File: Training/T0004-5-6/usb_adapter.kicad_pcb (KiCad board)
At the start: 2 copper layers, 50.8 x 25.4 mm, 23 parts, among them J1 modular8_rev3_comms_out, P1 USB_OTG, U1 FT231X, U2 TE_1825058-1

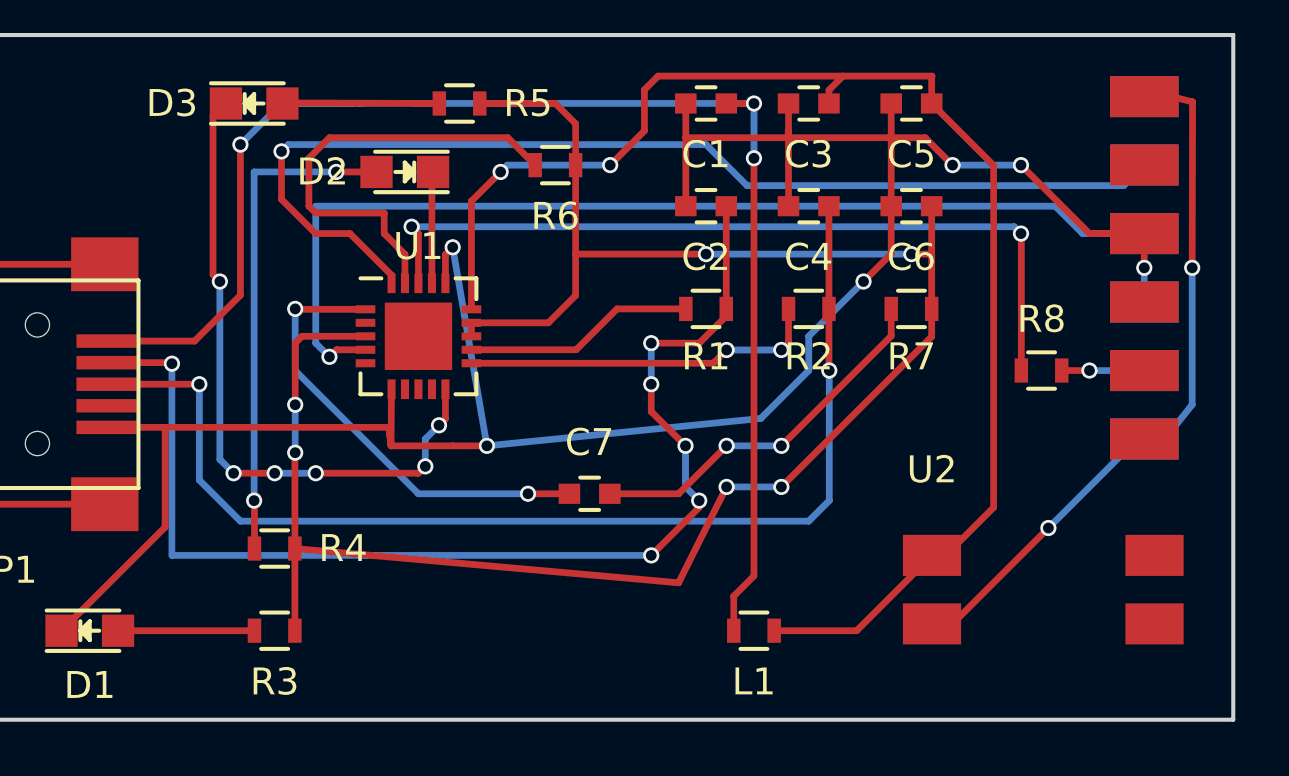
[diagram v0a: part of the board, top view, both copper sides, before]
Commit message: footprint updates and comments
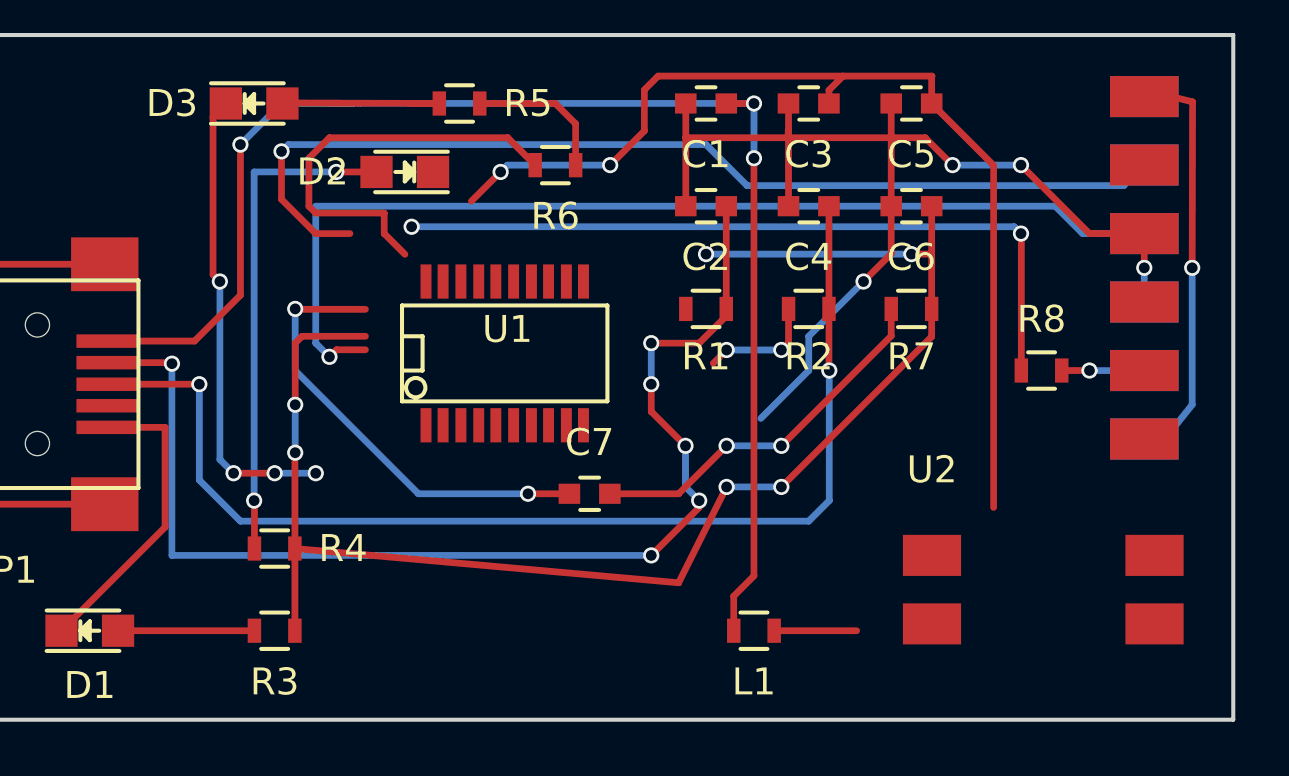
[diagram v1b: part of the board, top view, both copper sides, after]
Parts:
- U1: footprint Housings_DFN_QFN:QFN-20-1EP_4x4mm_Pitch0.5mm -> SMD_Packages:SSOP-20
- moved U1 3.26 mm to (161.7, 87.8)
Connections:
- U2 pad 1: +5V -> /POWER_OUT
- U2 pad 2: /POWER_OUT -> Net-(J1-Pad7)
- U2 pad 3: (no net) -> /PROGRAM
- U2 pad 4: (no net) -> +5V
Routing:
- net GND: track 88.7 -> 54.2 mm, vias 6 -> 4
- net +3V3: track 74.7 -> 60.2 mm
- net +5V: track 52.1 -> 41.1 mm
- net /POWER_OUT: track 26.2 -> 16.2 mm, vias 2 -> 1
- net Net-(R2-Pad1): track 13.3 -> 4.36 mm
- net Net-(R1-Pad1): track 8.58 -> 0.00 mm
- net /~TXLED: track 24.6 -> 17.3 mm, vias 6 -> 4
- net /~RXLED: track 4.15 -> 0.06 mm
- net /TX: track 40.4 -> 37.9 mm
- net /TXDEN: track 30.0 -> 27.8 mm
- net /~SLEEP: track 16.7 -> 15.7 mm
- net Net-(J1-Pad7): track 0.00 -> 0.76 mm

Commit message: finished routing after fix
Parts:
- moved C1 26.0 mm to (153.9, 99.6), turned to 270 degrees
- moved R4 24.9 mm to (178.1, 95.8), turned to 90 degrees
- moved C5 24.0 mm to (165.4, 99.6), turned to 270 degrees
- moved C4 23.6 mm to (156.2, 98.9), turned to 270 degrees
- moved R5 23.4 mm to (175.8, 95.8), turned to 90 degrees
- moved C6 23.1 mm to (160.8, 98.9), turned to 270 degrees
- moved D1 23.1 mm to (169.3, 96.0), turned to 90 degrees
- moved C3 22.7 mm to (163.1, 98.9), turned to 270 degrees
- moved R3 20.4 mm to (173.5, 95.8), turned to 90 degrees
- moved C2 19.8 mm to (158.5, 98.9), turned to 270 degrees
- moved D2 19.4 mm to (177.4, 80.4), turned to 0 degrees
- moved R2 19.4 mm to (156.0, 95.5), turned to 270 degrees
- moved D3 19.4 mm to (171.7, 80.4)
- moved L1 17.7 mm to (158.4, 85.6), turned to 270 degrees
- moved C7 17.1 mm to (181.9, 91.7)
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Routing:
- net Net-(C1-Pad1): track 51.8 -> 18.6 mm, vias 3 -> 2
- net Net-(C4-Pad1): track 42.2 -> 11.7 mm, vias 2 -> 0
- net Net-(C2-Pad1): track 43.9 -> 15.5 mm, vias 6 -> 0
- net /~RXLED: track 0.06 -> 20.2 mm, vias 0 -> 2
- net Net-(R1-Pad1): track 0.00 -> 18.6 mm, vias 0 -> 2
- net Net-(R2-Pad1): track 4.36 -> 22.0 mm
- net /RX: track 38.4 -> 22.2 mm
- net GND: track 54.2 -> 68.8 mm
- net /~TXLED: track 17.3 -> 2.82 mm, vias 4 -> 0
- net /POWER_OUT: track 16.2 -> 29.8 mm, vias 1 -> 2
- net Net-(J1-Pad7): track 0.76 -> 14.2 mm
- net /TXDEN: track 27.8 -> 15.3 mm
- net Net-(D3-Pad2): track 5.84 -> 17.0 mm, vias 0 -> 2
- net +3V3: track 60.2 -> 49.4 mm
- net /PROGRAM: track 13.9 -> 7.26 mm, vias 2 -> 0
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
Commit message: generated gerbers
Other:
- board text added: "USB to serial Jeremy OpenRobotics.ca"
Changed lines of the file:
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@@
     (area 142.164999 74.48957 195.793 104.48)
     (thickness 1.6)
-    (drawings 4)
+    (drawings 5)
     (tracks 202)
     (zones 0)
@@
     (visible_elements 7FFEFF7F)
     (pcbplotparams
-      (layerselection 0x00030_80000001)
-      (usegerberextensions false)
+      (layerselection 0x010f0_80000001)
+      (usegerberextensions true)
       (excludeedgelayer true)
       (linewidth 0.100000)
@@
       (outputformat 1)
       (mirror false)
-      (drillshape 1)
+      (drillshape 0)
       (scaleselection 1)
-      (outputdirectory ""))
+      (outputdirectory ../gerbers/Jeremy/))
   )
   (net 0 "")
@@
     (pad 4 smd rect (at 8.255 0 180) (size 2.159 1.524) (layers F.Cu F.Paste F.Mask)
       (net 4 +5V))
+  )
+  (gr_text "USB to serial\nJeremy\nOpenRobotics.ca" (at 143.256 80.264 180) (layer B.SilkS)
+    (effects (font (size 1 1) (thickness 0.1)) (justify left mirror))
   )
   (gr_line (start 193.04 76.962) (end 142.24 76.962) (angle 90) (layer Edge.Cuts) (width 0.15))
@@
   (segment (start 169.291 94.96298) (end 173.43698 94.96298) (width 0.25) (layer F.Cu) (net 9))
   (segment (start 173.43698 94.96298) (end 173.482 95.008) (width 0.25) (layer F.Cu) (net 9))
-  (segment (start 178.46802 80.391) (end 178.46802 84.67598) (width 0.25) (layer F.Cu) (net 10) (status 400000))
-  (segment (start 178.054 92.583) (end 178.054 95.008) (width 0.25) (layer F.Cu) (net 10) (status 800000))
+  (segment (start 178.46802 80.391) (end 178.46802 84.67598) (width 0.25) (layer F.Cu) (net 10))
+  (segment (start 178.054 92.583) (end 178.054 95.008) (width 0.25) (layer F.Cu) (net 10))
   (via (at 178.054 92.583) (size 0.6) (drill 0.4) (layers F.Cu B.Cu) (net 10))
   (segment (start 178.054 85.09) (end 178.054 92.583) (width 0.25) (layer B.Cu) (net 10))
@@
   (via (at 164.338 86.36) (size 0.6) (drill 0.4) (layers F.Cu B.Cu) (net 11))
   (segment (start 164.7952 86.8172) (end 164.338 86.36) (width 0.25) (layer F.Cu) (net 11))
-  (segment (start 172.75302 80.391) (end 174.625 80.391) (width 0.25) (layer F.Cu) (net 12) (status 400000))
-  (segment (start 175.768 92.583) (end 175.768 95.008) (width 0.25) (layer F.Cu) (net 12) (status 800000))
+  (segment (start 172.75302 80.391) (end 174.625 80.391) (width 0.25) (layer F.Cu) (net 12))
+  (segment (start 175.768 92.583) (end 175.768 95.008) (width 0.25) (layer F.Cu) (net 12))
   (via (at 175.768 92.583) (size 0.6) (drill 0.4) (layers F.Cu B.Cu) (net 12))
   (segment (start 175.768 85.471) (end 175.768 92.583) (width 0.25) (layer B.Cu) (net 12))
@@
   (segment (start 162.052 88.138) (end 165.989 88.138) (width 0.25) (layer F.Cu) (net 27))
   (segment (start 160.782 89.408) (end 162.052 88.138) (width 0.25) (layer F.Cu) (net 27))
-  (segment (start 165.989 87.4776) (end 168.2496 87.4776) (width 0.25) (layer F.Cu) (net 28) (status 400000))
-  (segment (start 174.244 87.122) (end 181.114 87.122) (width 0.25) (layer F.Cu) (net 28) (status 800000))
+  (segment (start 165.989 87.4776) (end 168.2496 87.4776) (width 0.25) (layer F.Cu) (net 28))
+  (segment (start 174.244 87.122) (end 181.114 87.122) (width 0.25) (layer F.Cu) (net 28))
   (segment (start 173.99 87.376) (end 174.244 87.122) (width 0.25) (layer F.Cu) (net 28))
   (via (at 173.99 87.376) (size 0.6) (drill 0.4) (layers F.Cu B.Cu) (net 28))

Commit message: generated gerbers
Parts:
- U1: value FT231X -> FT231XQ; footprint SMD_Packages:SSOP-20 -> Housings_DFN_QFN:QFN-20-1EP_4x4mm_Pitch0.5mm
- moved U2 49.9 mm to (141.0, 92.7), turned to 0 degrees
- moved C7 49.1 mm to (133.1, 85.9), turned to 90 degrees
- moved D2 49.1 mm to (133.1, 101.6)
- moved R4 48.7 mm to (130.3, 105.4)
- moved R3 46.7 mm to (127.8, 105.4)
- moved R7 44.9 mm to (140.4, 106.7)
- moved R5 44.0 mm to (132.8, 105.4)
- moved D3 40.7 mm to (136.9, 101.6)
- moved D1 40.4 mm to (129.3, 101.6), turned to 180 degrees
- moved C5 40.1 mm to (128.3, 84.3), turned to 90 degrees
- moved C3 40.0 mm to (125.7, 84.6), turned to 90 degrees
- moved U1 39.8 mm to (130.2, 96.1), turned to 270 degrees
- moved C2 38.1 mm to (123.2, 84.6), turned to 90 degrees
- moved R1 37.4 mm to (122.4, 105.4)
- moved R8 37.0 mm to (146.8, 99.1)
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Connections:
- U1 pad 1: Net-(C7-Pad1) -> /RX
- U1 pad 10: /~TXLED -> +3V3
- U1 pad 11: Net-(R2-Pad1) -> +3V3
- U1 pad 12: Net-(R1-Pad1) -> +5V
- U1 pad 13: +3V3 -> GND
- U1 pad 14: +3V3 -> /~RXLED
- U1 pad 15: +5V -> /TXDEN
- U1 pad 16: GND -> /~SLEEP
- U1 pad 17: /~RXLED -> /TX
- U1 pad 18: /TXDEN -> Net-(C7-Pad1)
- U1 pad 19: /~SLEEP -> Net-(U1-Pad19)
- U1 pad 20: /TX -> +3V3
- U1 pad 3: +3V3 -> GND
- U1 pad 4: /RX -> Net-(U1-Pad4)
- U1 pad 6: GND -> Net-(U1-Pad6)
- U1 pad 7: Net-(U1-Pad7) -> /~TXLED
- U1 pad 8: Net-(U1-Pad8) -> Net-(R2-Pad1)
- U1 pad 9: Net-(U1-Pad9) -> Net-(R1-Pad1)
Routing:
- net GND: track 68.8 -> 108.7 mm, vias 4 -> 6
- net /PROGRAM: track 7.26 -> 39.6 mm, vias 0 -> 3
- net /~TXLED: track 2.82 -> 24.9 mm, vias 0 -> 2
- net Net-(C4-Pad1): track 11.7 -> 31.3 mm, vias 0 -> 2
- net /~RXLED: track 20.2 -> 4.07 mm, vias 2 -> 0
- net Net-(C1-Pad1): track 18.6 -> 34.1 mm
- net /RX: track 22.2 -> 37.3 mm, vias 1 -> 3
- net /TX: track 44.3 -> 33.4 mm
- net Net-(C2-Pad1): track 15.5 -> 26.0 mm
- net Net-(D3-Pad2): track 17.0 -> 6.92 mm, vias 2 -> 0
- net Net-(D2-Pad2): track 14.8 -> 5.16 mm, vias 2 -> 0
- net Net-(R2-Pad1): track 22.0 -> 13.9 mm, vias 2 -> 0
- net +5V: track 41.5 -> 48.3 mm
- net Net-(J1-Pad7): track 14.2 -> 19.4 mm, vias 0 -> 2
- net /POWER_OUT: track 29.8 -> 33.7 mm, vias 2 -> 3
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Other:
- board text removed: "USB to serial Jeremy OpenRobotics.ca"

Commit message: generated gerbers
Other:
- board text added: "USB to serial Jeremy OpenRobotics.ca"
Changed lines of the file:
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@@
     (area 108.833839 82.223571 163.535 108.475)
     (thickness 1.6)
-    (drawings 4)
+    (drawings 5)
     (tracks 286)
     (zones 0)
@@
       (net 14 /POWER_OUT))
   )
+  (gr_text "USB to serial\nJeremy\nOpenRobotics.ca" (at 111.506 85.598 180) (layer B.SilkS)
+    (effects (font (size 1 1) (thickness 0.1)) (justify left mirror))
+  )
   (gr_line (start 161.29 82.55) (end 161.29 107.95) (layer Edge.Cuts) (width 0.15))
